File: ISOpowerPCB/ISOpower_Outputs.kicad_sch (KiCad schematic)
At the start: 20 parts, among them J10 USB_CH_A, J11 USB_CH_A, J12 USB_CH_A, J13 USB_CH_A, J14 XT30_connector_DC_30A_female, J15 XT30_connector_DC_30A_female, J16 XT30_connector_DC_30A_female, J17 XT30_connector_DC_30A_female, J18 XT30_connector_DC_30A_female, J9 USB_CH_A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

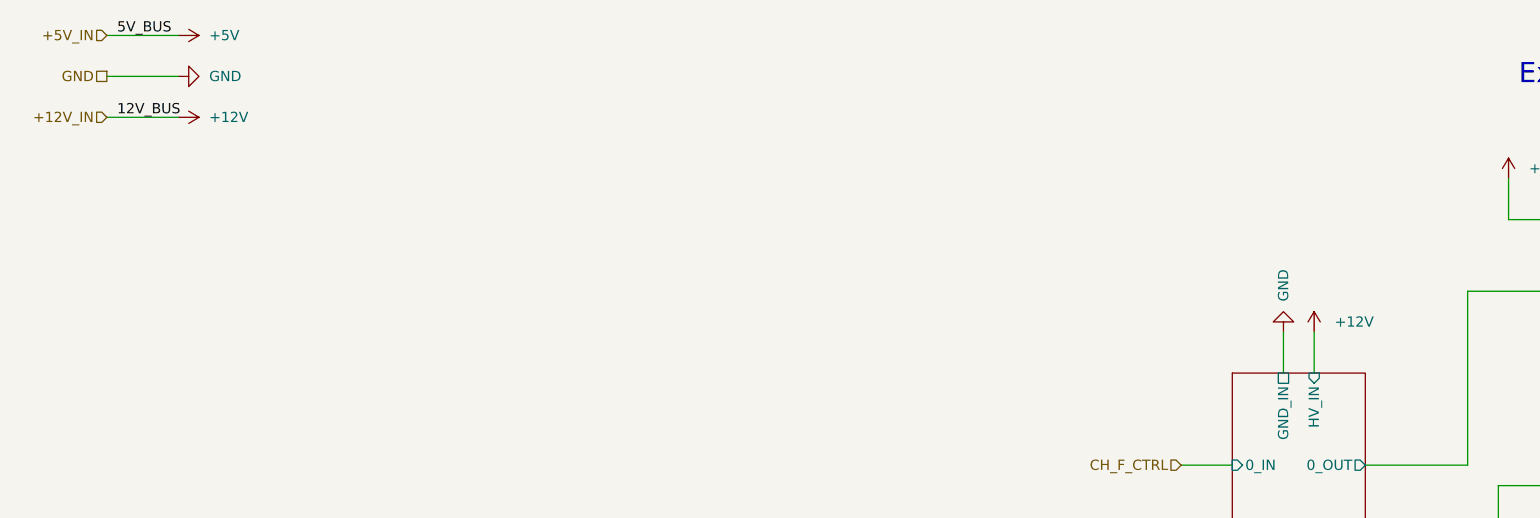
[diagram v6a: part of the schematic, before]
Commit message: PCB layout completed.
Screenshots added to media folder
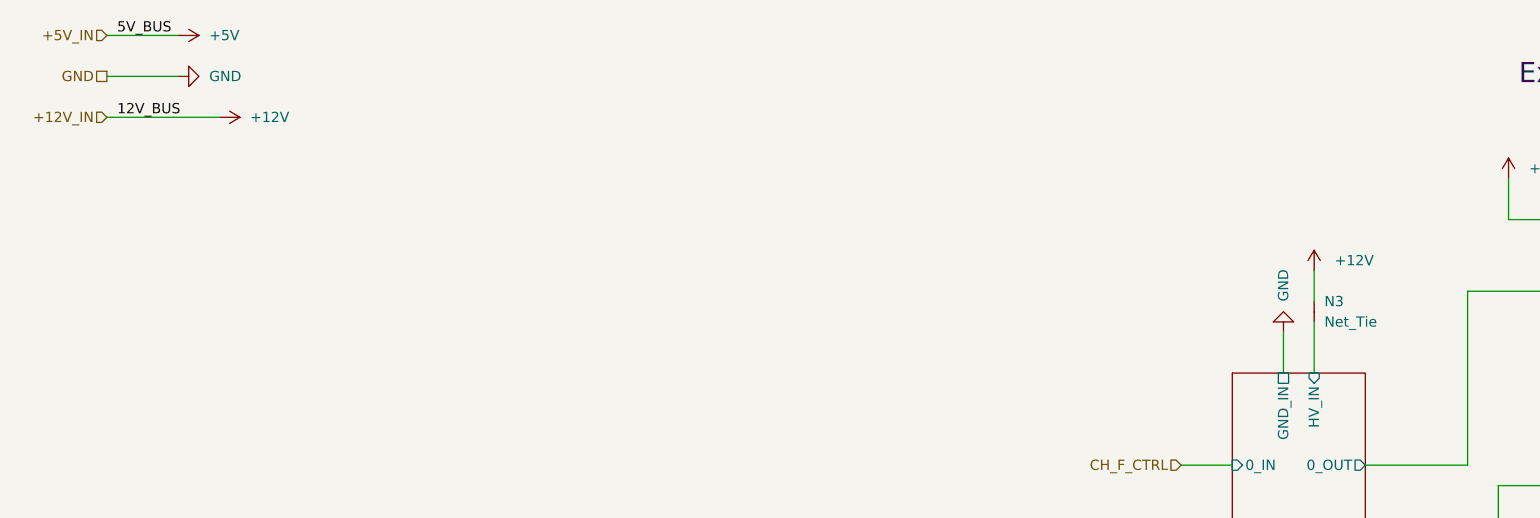
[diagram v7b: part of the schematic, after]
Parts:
- added N3: Net_Tie, NetTie:NetTie-2_SMD_Pad0.5mm, symbol 000_Utility_Immo:Net_Tie
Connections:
- net +12V: now also N3.2 (C)
- new net 5v to 12v logic conversion_v2/HV_IN: N3.1 (A)
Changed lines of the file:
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@@
+    (stroke (width 0) (type default) (color 0 0 0 0))
+  )
+  (wire (pts (xy 172.72 48.26) (xy 172.72 52.07))
     (stroke (width 0) (type default) (color 0 0 0 0))
   )
@@
     (stroke (width 0) (type default) (color 0 0 0 0))
   )
-  (wire (pts (xy 22.86 29.21) (xy 31.75 29.21))
+  (wire (pts (xy 22.86 29.21) (xy 36.83 29.21))
     (stroke (width 0) (type default) (color 0 0 0 0))
   )
@@
     (stroke (width 0) (type default) (color 0 0 0 0))
   )
+  (wire (pts (xy 172.72 54.61) (xy 172.72 60.96))
+    (stroke (width 0) (type default) (color 0 0 0 0))
+  )
   (wire (pts (xy 102.87 128.27) (xy 109.22 128.27))
     (stroke (width 0) (type default) (color 0 0 0 0))
@@
   )
   (wire (pts (xy 245.11 44.45) (xy 245.11 64.77))
-    (stroke (width 0) (type default) (color 0 0 0 0))
-  )
-  (wire (pts (xy 172.72 55.88) (xy 172.72 60.96))
     (stroke (width 0) (type default) (color 0 0 0 0))
   )
@@
     (pin "1")
   )
-  (symbol (lib_id "power:+12V") (at 31.75 29.21 270) (unit 1)
-    (in_bom yes) (on_board yes) (fields_autoplaced)
-    (property "Reference" "#PWR054" (id 0) (at 27.94 29.21 0)
-      (effects (font (size 1.27 1.27)) hide)
-    )
-    (property "Value" "+12V" (id 1) (at 35.56 29.2099 90)
+  (symbol (lib_id "power:+12V") (at 36.83 29.21 270) (unit 1)
+    (in_bom yes) (on_board yes) (fields_autoplaced)
+    (property "Reference" "#PWR054" (id 0) (at 33.02 29.21 0)
+      (effects (font (size 1.27 1.27)) hide)
+    )
+    (property "Value" "+12V" (id 1) (at 40.64 29.2099 90)
       (effects (font (size 1.27 1.27)) (justify left))
     )
-    (property "Footprint" "" (id 2) (at 31.75 29.21 0)
-      (effects (font (size 1.27 1.27)) hide)
-    )
-    (property "Datasheet" "" (id 3) (at 31.75 29.21 0)
+    (property "Footprint" "" (id 2) (at 36.83 29.21 0)
+      (effects (font (size 1.27 1.27)) hide)
+    )
+    (property "Datasheet" "" (id 3) (at 36.83 29.21 0)
       (effects (font (size 1.27 1.27)) hide)
     )
@@
     (pin "1")
   )
+  (symbol (lib_id "000_Utility_Immo:Net_Tie") (at 172.72 53.34 90) (unit 1)
+    (in_bom no) (on_board yes) (fields_autoplaced)
+    (property "Reference" "N3" (id 0) (at 173.99 52.0699 90)
+      (effects (font (size 1.27 1.27)) (justify right))
+    )
+    (property "Value" "Net_Tie" (id 1) (at 173.99 54.6099 90)
+      (effects (font (size 1.27 1.27)) (justify right))
+    )
+    (property "Footprint" "NetTie:NetTie-2_SMD_Pad0.5mm" (id 2) (at 175.26 53.34 0)
+      (effects (font (size 1.27 1.27)) hide)
+    )
+    (property "Datasheet" "~" (id 3) (at 171.45 53.34 0)
+      (effects (font (size 1.27 1.27)) hide)
+    )
+    (pin "1")
+    (pin "2")
+  )
   (symbol (lib_id "000_MOSFET_Immo:IRF5305_PBF") (at 228.6 139.7 270) (mirror x) (unit 1)
     (in_bom yes) (on_board yes)
@@
     (pin "1")
   )
-  (symbol (lib_id "power:+12V") (at 172.72 55.88 0) (unit 1)
-    (in_bom yes) (on_board yes) (fields_autoplaced)
-    (property "Reference" "#PWR066" (id 0) (at 172.72 59.69 0)
-      (effects (font (size 1.27 1.27)) hide)
-    )
-    (property "Value" "+12V" (id 1) (at 175.26 54.6099 0)
+  (symbol (lib_id "power:+12V") (at 172.72 48.26 0) (unit 1)
+    (in_bom yes) (on_board yes) (fields_autoplaced)
+    (property "Reference" "#PWR066" (id 0) (at 172.72 52.07 0)
+      (effects (font (size 1.27 1.27)) hide)
+    )
+    (property "Value" "+12V" (id 1) (at 175.26 46.9899 0)
       (effects (font (size 1.27 1.27)) (justify left))
     )
-    (property "Footprint" "" (id 2) (at 172.72 55.88 0)
-      (effects (font (size 1.27 1.27)) hide)
-    )
-    (property "Datasheet" "" (id 3) (at 172.72 55.88 0)
-      (effects (font (size 1.27 1.27)) hide)
-    )
+    (property "Footprint" "" (id 2) (at 172.72 48.26 0)
+      (effects (font (size 1.27 1.27)) hide)
+    )
+    (property "Datasheet" "" (id 3) (at 172.72 48.26 0)
+      (effects (font (size 1.27 1.27)) hide)
+    )

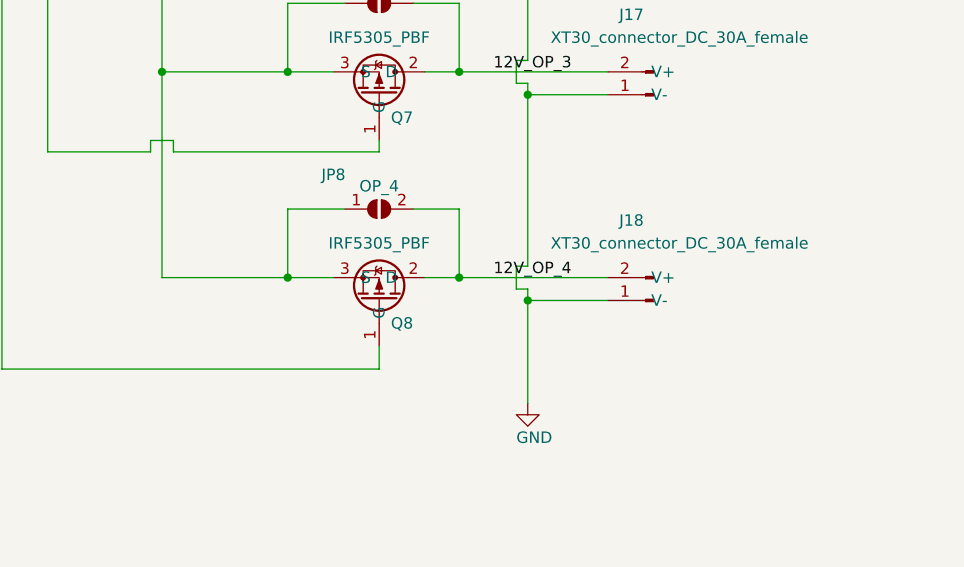
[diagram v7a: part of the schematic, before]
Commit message: Replacing power bus RE current draw issue
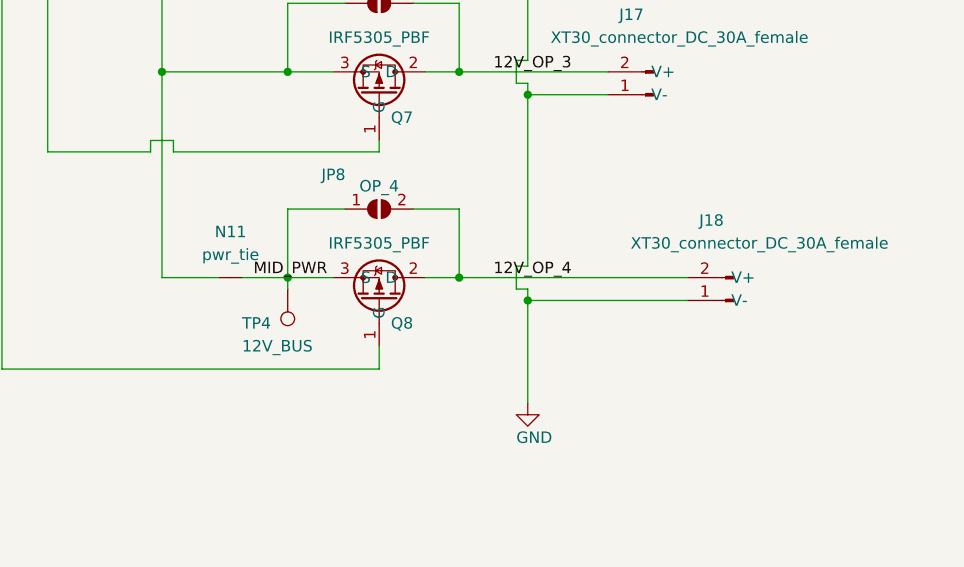
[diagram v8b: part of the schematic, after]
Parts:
- added N11: pwr_tie, NetTie:NetTie-8-15A_1oz_2oz, symbol 000_Utility_Immo:pwr_tie
- added TP4: 12V_BUS, TestPoint:TestPoint_Pad_D1.5mm, symbol Connector:TestPoint
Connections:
- net +12V: now also N11.1 (A); no longer JP8.1 (A), Q8.3 (S)
- new net MID_PWR: JP8.1 (A), N11.2 (C), Q8.3 (S), TP4.1
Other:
- moved on the sheet: J18
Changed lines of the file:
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@@
   (junction (at 218.44 66.04) (diameter 0) (color 0 0 0 0)
   )
+  (junction (at 204.47 114.3) (diameter 0) (color 0 0 0 0)
+  )
+  (junction (at 116.84 146.05) (diameter 0) (color 0 0 0 0)
+  )
+  (junction (at 204.47 41.91) (diameter 0) (color 0 0 0 0)
+  )
+  (junction (at 245.11 116.84) (diameter 0) (color 0 0 0 0)
+  )
+  (junction (at 245.11 139.7) (diameter 0) (color 0 0 0 0)
+  )
+  (junction (at 219.71 41.91) (diameter 0) (color 0 0 0 0)
+  )
+  (junction (at 237.49 41.91) (diameter 0) (color 0 0 0 0)
+  )
+  (junction (at 245.11 92.71) (diameter 0) (color 0 0 0 0)
+  )
   (junction (at 218.44 137.16) (diameter 0) (color 0 0 0 0)
   )
-  (junction (at 204.47 114.3) (diameter 0) (color 0 0 0 0)
-  )
-  (junction (at 116.84 146.05) (diameter 0) (color 0 0 0 0)
-  )
-  (junction (at 204.47 41.91) (diameter 0) (color 0 0 0 0)
-  )
-  (junction (at 245.11 116.84) (diameter 0) (color 0 0 0 0)
-  )
-  (junction (at 245.11 139.7) (diameter 0) (color 0 0 0 0)
-  )
-  (junction (at 219.71 41.91) (diameter 0) (color 0 0 0 0)
-  )
-  (junction (at 237.49 41.91) (diameter 0) (color 0 0 0 0)
-  )
-  (junction (at 245.11 92.71) (diameter 0) (color 0 0 0 0)
-  )
   (junction (at 237.49 90.17) (diameter 0) (color 0 0 0 0)
   )
@@
   (junction (at 218.44 90.17) (diameter 0) (color 0 0 0 0)
   )
+  (junction (at 53.34 146.05) (diameter 0) (color 0 0 0 0)
+  )
   (junction (at 237.49 137.16) (diameter 0) (color 0 0 0 0)
-  )
-  (junction (at 53.34 146.05) (diameter 0) (color 0 0 0 0)
   )
   (junction (at 245.11 68.58) (diameter 0) (color 0 0 0 0)
@@
     (stroke (width 0) (type default) (color 0 0 0 0))
   )
+  (wire (pts (xy 213.36 137.16) (xy 218.44 137.16))
+    (stroke (width 0) (type default) (color 0 0 0 0))
+  )
   (wire (pts (xy 156.21 95.25) (xy 162.56 95.25))
     (stroke (width 0) (type default) (color 0 0 0 0))
@@
     (stroke (width 0) (type default) (color 0 0 0 0))
   )
+  (wire (pts (xy 218.44 138.43) (xy 218.44 137.16))
+    (stroke (width 0) (type default) (color 0 0 0 0))
+  )
   (wire (pts (xy 196.85 36.83) (xy 196.85 41.91))
     (stroke (width 0) (type default) (color 0 0 0 0))
@@
     (stroke (width 0) (type default) (color 0 0 0 0))
   )
-  (wire (pts (xy 237.49 137.16) (xy 254 137.16))
-    (stroke (width 0) (type default) (color 0 0 0 0))
-  )
   (wire (pts (xy 204.47 114.3) (xy 204.47 137.16))
     (stroke (width 0) (type default) (color 0 0 0 0))
@@
     (stroke (width 0) (type default) (color 0 0 0 0))
   )
+  (wire (pts (xy 237.49 137.16) (xy 262.89 137.16))
+    (stroke (width 0) (type default) (color 0 0 0 0))
+  )
   (wire (pts (xy 219.71 34.29) (xy 224.79 34.29))
     (stroke (width 0) (type default) (color 0 0 0 0))
@@
     (stroke (width 0) (type default) (color 0 0 0 0))
   )
+  (wire (pts (xy 204.47 137.16) (xy 210.82 137.16))
+    (stroke (width 0) (type default) (color 0 0 0 0))
+  )
   (wire (pts (xy 102.87 128.27) (xy 109.22 128.27))
     (stroke (width 0) (type default) (color 0 0 0 0))
   )
-  (wire (pts (xy 245.11 139.7) (xy 254 139.7))
+  (wire (pts (xy 245.11 139.7) (xy 262.89 139.7))
     (stroke (width 0) (type default) (color 0 0 0 0))
   )
@@
   )
   (wire (pts (xy 228.6 97.79) (xy 228.6 99.06))
-    (stroke (width 0) (type default) (color 0 0 0 0))
-  )
-  (wire (pts (xy 204.47 137.16) (xy 218.44 137.16))
     (stroke (width 0) (type default) (color 0 0 0 0))
   )
@@
   )
   (label "12V_OP_4" (at 241.3 137.16 0)
+    (effects (font (size 1.27 1.27)) (justify left bottom))
+  )
+  (label "MID_PWR" (at 214.63 137.16 0)
     (effects (font (size 1.27 1.27)) (justify left bottom))
   )
@@
     (pin "1")
   )
+  (symbol (lib_id "Connector:TestPoint") (at 218.44 138.43 180) (unit 1)
+    (in_bom yes) (on_board yes)
+    (property "Reference" "TP4" (id 0) (at 213.36 142.24 0)
+      (effects (font (size 1.27 1.27)) (justify right))
+    )
+    (property "Value" "12V_BUS" (id 1) (at 213.36 144.78 0)
+      (effects (font (size 1.27 1.27)) (justify right))
+    )
+    (property "Footprint" "TestPoint:TestPoint_Pad_D1.5mm" (id 2) (at 213.36 138.43 0)
+      (effects (font (size 1.27 1.27)) hide)
+    )
+    (property "Datasheet" "~" (id 3) (at 213.36 138.43 0)
+      (effects (font (size 1.27 1.27)) hide)
+    )
+    (pin "1")
+  )
   (symbol (lib_id "000_MOSFET_Immo:IRF5305_PBF") (at 228.6 68.58 270) (mirror x) (unit 1)
     (in_bom yes) (on_board yes)
@@
     (pin "1")
   )
+  (symbol (lib_id "000_Utility_Immo:pwr_tie") (at 212.09 137.16 0) (unit 1)
+    (in_bom no) (on_board yes) (fields_autoplaced)
+    (property "Reference" "N11" (id 0) (at 212.09 132.08 0))
+    (property "Value" "pwr_tie" (id 1) (at 212.09 134.62 0))
+    (property "Footprint" "NetTie:NetTie-8-15A_1oz_2oz" (id 2) (at 212.09 139.7 0)
+      (effects (font (size 1.27 1.27)) hide)
+    )
+    (property "Datasheet" "~" (id 3) (at 212.09 135.89 0)
+      (effects (font (size 1.27 1.27)) hide)
+    )
+    (pin "1")
+    (pin "2")
+  )
   (symbol (lib_id "000_Connectors_Immo:XT30_connector_DC_30A_female") (at 259.08 92.71 180) (unit 1)
     (in_bom yes) (on_board yes)
@@
     (pin "1")
   )
-  (symbol (lib_id "000_Connectors_Immo:XT30_connector_DC_30A_female") (at 259.08 139.7 180) (unit 1)
+  (symbol (lib_id "000_Connectors_Immo:XT30_connector_DC_30A_female") (at 267.97 139.7 180) (unit 1)
     (in_bom yes) (on_board yes)
-    (property "Reference" "J18" (id 0) (at 255.27 130.81 0)
-      (effects (font (size 1.27 1.27)) (justify right))
-    )
-    (property "Value" "XT30_connector_DC_30A_female" (id 1) (at 247.65 133.35 0)
-      (effects (font (size 1.27 1.27)) (justify right))
-    )
-    (property "Footprint" "Connector_AMASS:AMASS_XT30PW-F_1x02_P2.50mm_Horizontal" (id 2) (at 259.08 139.7 0)
-      (effects (font (size 1.27 1.27)) hide)
-    )
-    (property "Datasheet" "~" (id 3) (at 261.62 139.7 90)
-      (effects (font (size 1.27 1.27)) hide)
-    )
+    (property "Reference" "J18" (id 0) (at 264.16 130.81 0)
+      (effects (font (size 1.27 1.27)) (justify right))
+    )
+    (property "Value" "XT30_connector_DC_30A_female" (id 1) (at 256.54 133.35 0)
+      (effects (font (size 1.27 1.27)) (justify right))
+    )
+    (property "Footprint" "Connector_AMASS:AMASS_XT30PW-F_1x02_P2.50mm_Horizontal" (id 2) (at 267.97 139.7 0)
+      (effects (font (size 1.27 1.27)) hide)
+    )
+    (property "Datasheet" "~" (id 3) (at 270.51 139.7 90)
+      (effects (font (size 1.27 1.27)) hide)
+    )
